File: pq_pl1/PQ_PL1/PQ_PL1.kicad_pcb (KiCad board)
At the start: 2 copper layers, 40 x 40 mm, 9 parts, among them J1 Conn_01x10, J2 Conn_01x10, J4 Conn_01x10, U1 PTC06

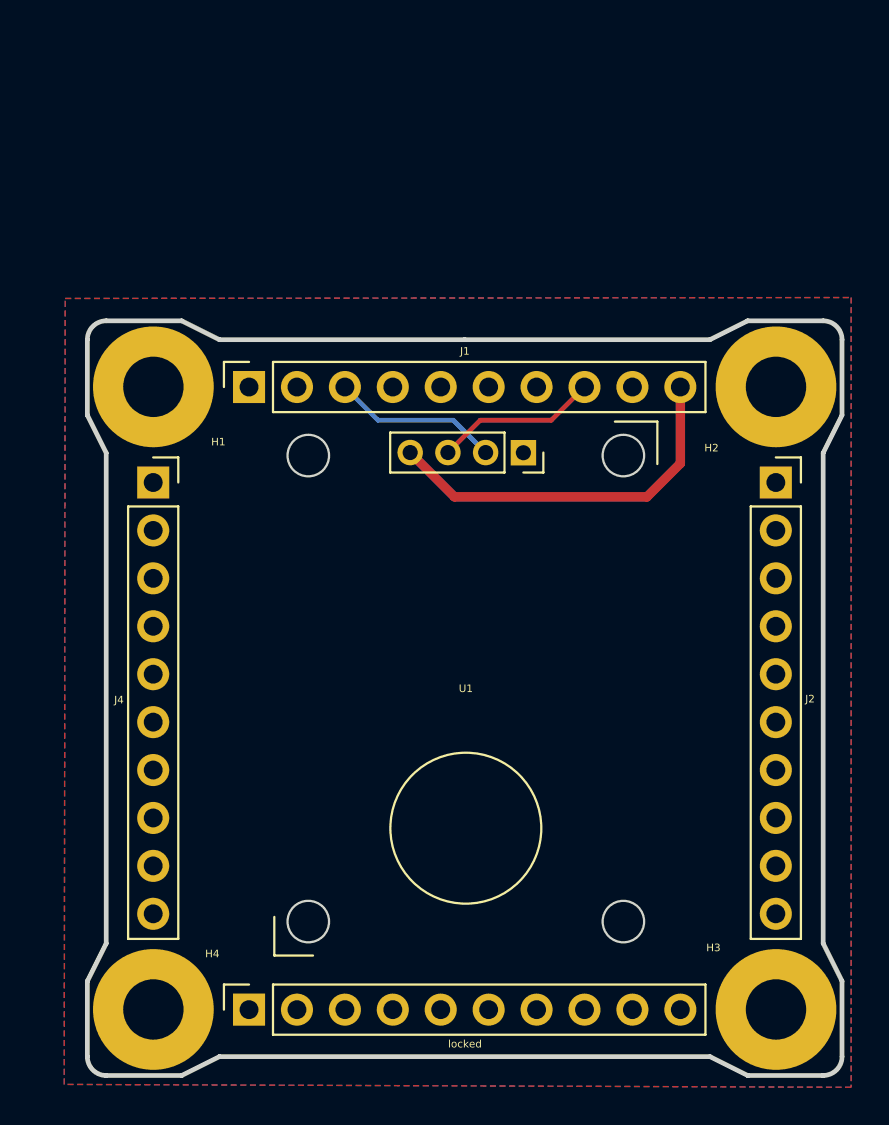
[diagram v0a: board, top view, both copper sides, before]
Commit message: Full Kicad7 transition, library improvement and adaptation, correct footprints and 3D models added
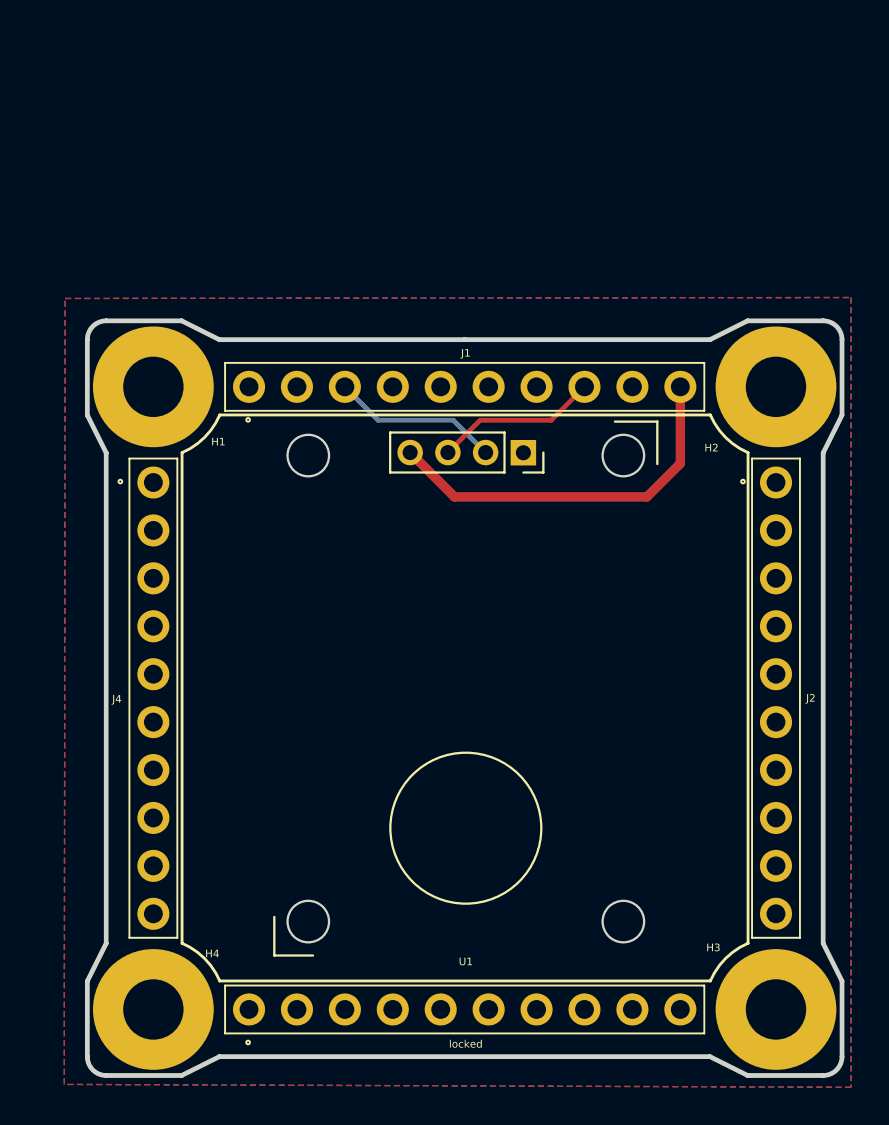
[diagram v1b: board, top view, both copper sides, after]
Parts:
- J1, J2, J4, locked: footprint connector-nsl:SLW-110-01 -> -nsl_connector:BBL-110-Y-X
- U1: footprint sensor-nsl:PTC06 -> -nsl_sensor:PTC06
- turned J1 to 0 degrees
- turned J2 to -90 degrees
- turned J4 to -90 degrees
- turned locked to 0 degrees

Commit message: pl1 ready to manufacture, obc&comms small touches prior to manufacture
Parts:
- moved locked 25.2 mm to (111.4, 66.5), turned to 180 degrees
- moved U1 15.1 mm to (100.1, 49.5)
- moved H1 15.1 mm to (83.5, 33.5)
- moved H2 15.1 mm to (116.5, 33.5)
- moved H3 15.1 mm to (116.5, 66.5)
- moved H4 15.1 mm to (83.5, 66.5)
- moved J1 15.1 mm to (88.6, 33.5)
- moved J2 15.1 mm to (116.5, 38.6)
- moved J4 8.37 mm to (83.5, 61.4), turned to 90 degrees
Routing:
- net /3V3_PERM: track 20.1 -> 20.6 mm

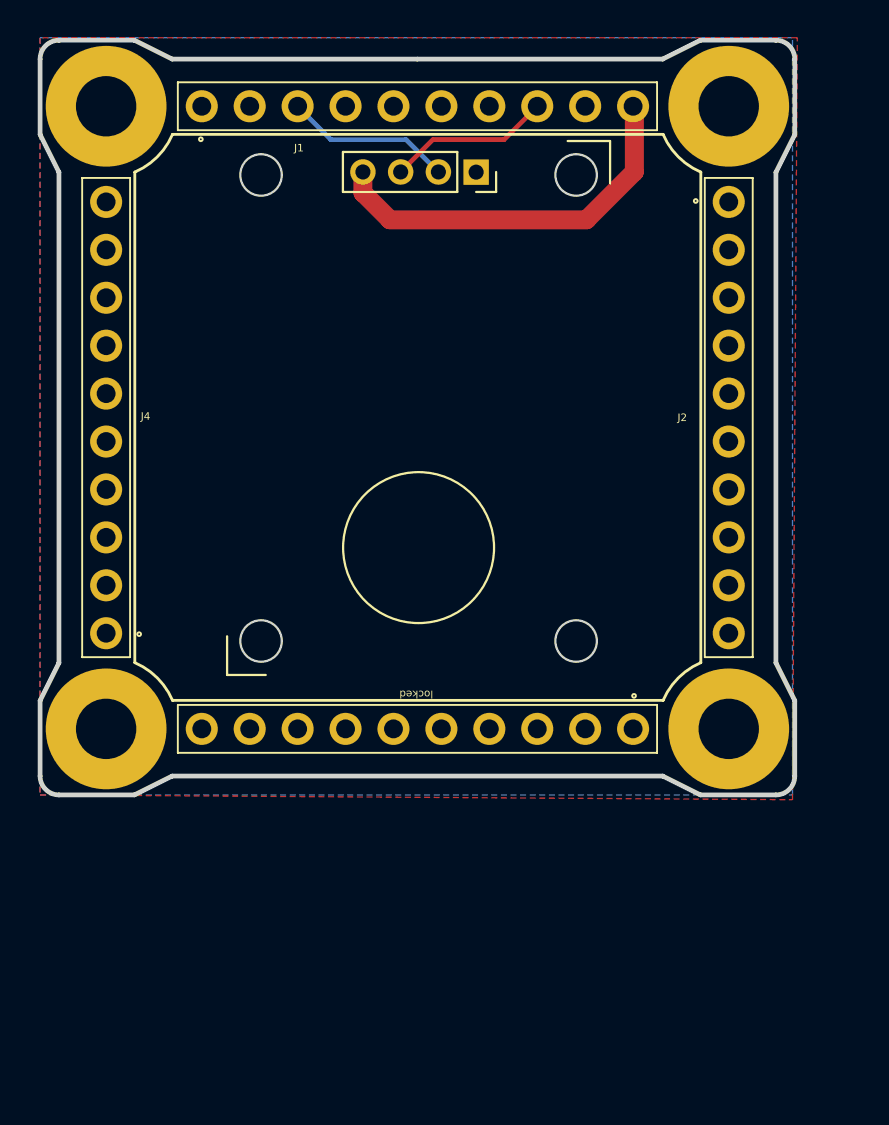
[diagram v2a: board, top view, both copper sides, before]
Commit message: Payload 1 board vertical connector silkscreen annotation correction
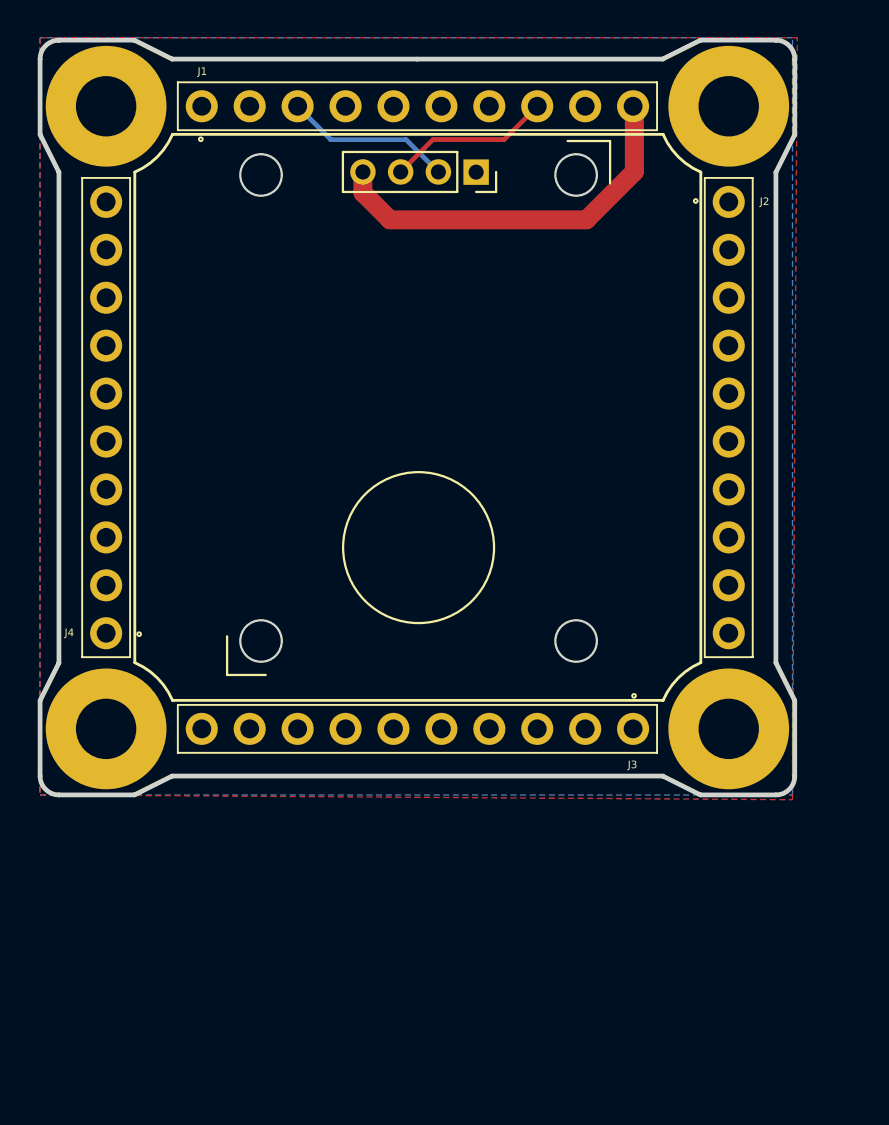
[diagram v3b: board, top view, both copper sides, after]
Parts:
- renumbered locked to J3
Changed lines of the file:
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@@
     (property "ki_keywords" "connector")
     (attr through_hole)
-    (fp_text reference "J2" (at 11.43 2.464 unlocked) (layer "F.SilkS")
+    (fp_text reference "J2" (at -0.02 -1.9 unlocked) (layer "F.SilkS")
         (effects (font (size 0.4 0.4) (thickness 0.15)))
     )
@@
     (property "ki_keywords" "connector")
     (attr through_hole)
-    (fp_text reference "J1" (at 5.146 2.21 unlocked) (layer "F.SilkS")
+    (fp_text reference "J1" (at 0.03 -1.85 unlocked) (layer "F.SilkS")
         (effects (font (size 0.4 0.4) (thickness 0.15)))
     )
@@
         (effects (font (size 1.27 1.27) (thickness 0.254)))
     )
-    (fp_text user "${REFERENCE}" (at 11.4908 0.0408) (layer "F.Fab")
+    (fp_text user "${REFERENCE}" (at 3.78 0.4) (layer "F.Fab")
         (effects (font (size 1.27 1.27) (thickness 0.254)))
     )
@@
     (property "ki_keywords" "connector")
     (attr through_hole)
-    (fp_text reference "J4" (at 11.496 2.088 unlocked) (layer "F.SilkS")
+    (fp_text reference "J4" (at 0.03 -1.95 unlocked) (layer "F.SilkS")
         (effects (font (size 0.4 0.4) (thickness 0.15)))
     )
@@
     (property "ki_keywords" "connector")
     (attr through_hole)
-    (fp_text reference locked "J3" (at 11.4908 1.8388 180 unlocked) (layer "F.SilkS")
-        (effects (font (size 0.4 0.4) (thickness 0.15)))
-    )
+    (fp_text reference "J3" (at 0.03 -1.9 unlocked) (layer "F.SilkS")
+        (effects (font (size 0.4 0.4) (thickness 0.15)))
+    )
